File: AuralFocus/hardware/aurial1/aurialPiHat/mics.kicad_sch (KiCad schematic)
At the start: 7 parts, among them J1 Conn_01x05_Pin

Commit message: Muitas mudanças no circuito, clocks no stm32h7 e mais,
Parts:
- renumbered C2 to C1, C1 to C2, MK7 to MK1
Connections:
- net GND: no longer MK1.5 (GND)
- net VDD: no longer MK1.2 (VDD)
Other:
- note added: "Para SNR máximo do IM69D130 (69 dB(A)), adicione capacitor de bypass de 100 nF diretamente no pin VDD de cada microfone (<1 mm de distância) - o datasheet recomenda isso para melhor SNR."
- moved on the sheet: C1, C2, J1

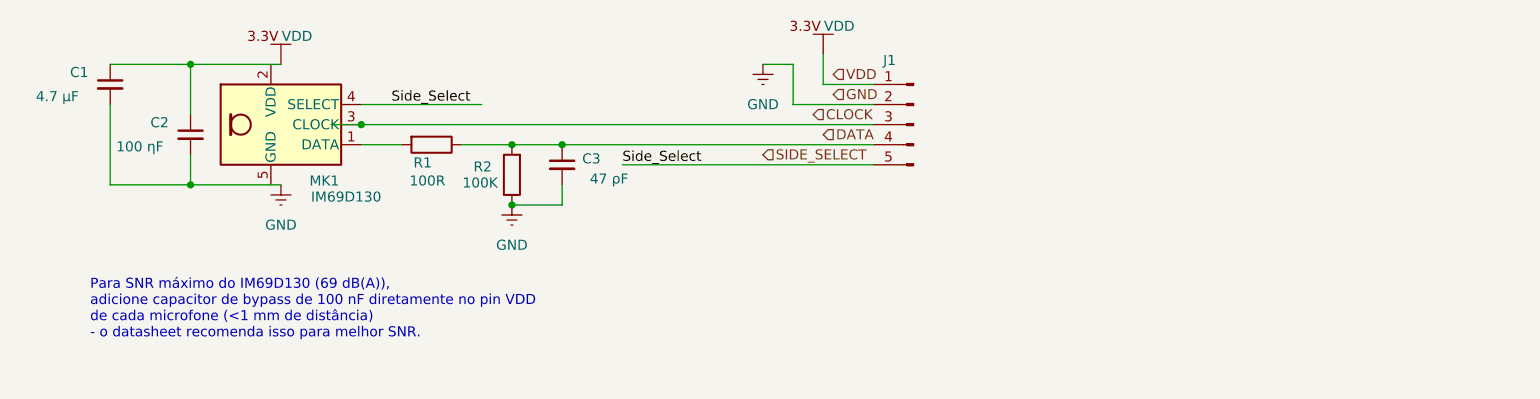
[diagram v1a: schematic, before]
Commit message: correções, VDD, VSS e outros pinos relevantes para contexto.
 ### Decoupling Strategy for STM32H753 Power Pins

 The STM32H753 microcontroller is a high-performance Cortex-M7 device operating at up to 480 MHz, with integrated USB High-Speed functionality. Such high-speed operation demands a robust power supply decoupling strategy to ensure signal integrity and minimize electromagnetic interference (EMI). Below is the detailed decoupling approach implemented in the AuralFocus HAT design:

 **1. Global Power Filtering**
 - **Ferrite Bead (FB3 - 600 Ω @ 100 MHz)**: placed on the main 3.3 V supply line feeding the STM32H753. This ferrite bead attenuates high-frequency noise originating from upstream sources (e.g., Raspberry Pi power supply, servo motors) before it reaches the microcontroller.
 - **Post-Ferrite Capacitor Bank**:
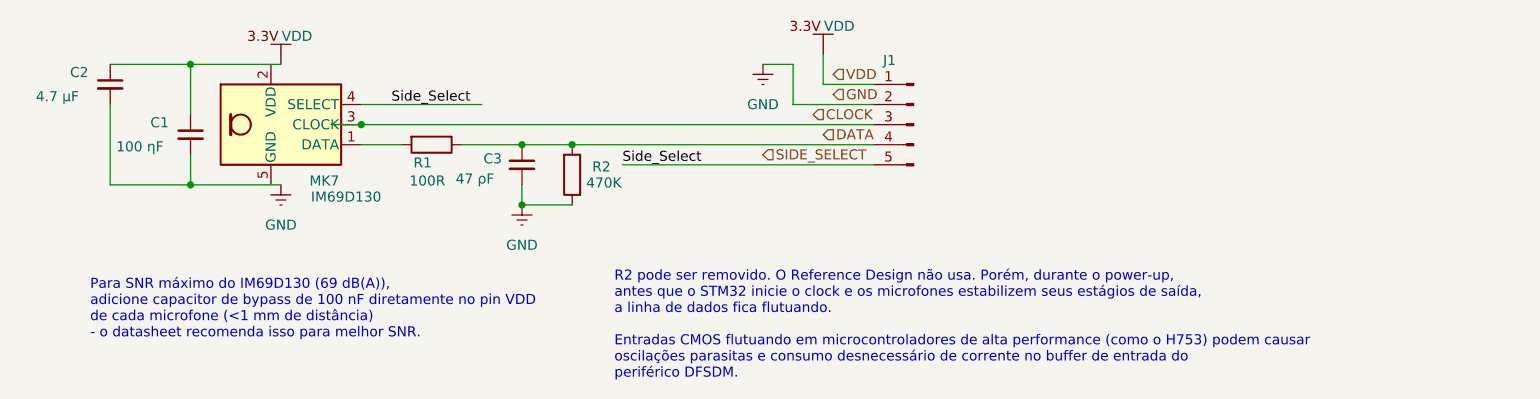
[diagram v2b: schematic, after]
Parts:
- R2: value 100K -> 470K
- renumbered C2 to C1, C1 to C2, MK1 to MK7
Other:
- note added: "R2 pode ser removido. O Reference Design não usa. Porém, durante o power-up, antes que o STM32 inicie o clock e os microfones estabilizem seus estágios de saída, a linha de dados fica flutuando. Entradas CMOS flutuando em microcontroladores de alta performance (como o H753) podem causar oscilações parasitas e consumo desnecessário de corrente no buffer de entrada do periférico DFSDM."
- moved on the sheet: C3, R2
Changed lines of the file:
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@@
 	(generator_version "9.0")
 	(paper "A4")
+	(text "R2 pode ser removido. O Reference Design não usa. Porém, durante o power-up, \nantes que o STM32 inicie o clock e os microfones estabilizem seus estágios de saída, \na linha de dados fica flutuando. \n\nEntradas CMOS flutuando em microcontroladores de alta performance (como o H753) podem causar \noscilações parasitas e consumo desnecessário de corrente no buffer de entrada do \nperiférico DFSDM."
+		(exclude_from_sim no)
+		(at 162.814 128.27 0)
+		(effects
+			(font
+				(size 1.27 1.27)
+			)
+			(justify left)
+		)
+	)
 	(text "Para SNR máximo do IM69D130 (69 dB(A)), \nadicione capacitor de bypass de 100 nF diretamente no pin VDD \nde cada microfone (<1 mm de distância) \n- o datasheet recomenda isso para melhor SNR."
 		(exclude_from_sim no)
@@
 	)
 	(junction
-		(at 149.86 113.03)
-		(diameter 0)
-		(color 0 0 0 0)
-	)
-	(junction
 		(at 109.22 95.25)
-		(diameter 0)
-		(color 0 0 0 0)
-	)
-	(junction
-		(at 156.21 105.41)
 		(diameter 0)
 		(color 0 0 0 0)
@@
 	)
 	(junction
-		(at 149.86 105.41)
+		(at 151.13 113.03)
 		(diameter 0)
 		(color 0 0 0 0)
@@
 		(color 0 0 0 0)
 	)
-	(wire
-		(pts
-			(xy 143.51 105.41) (xy 149.86 105.41)
+	(junction
+		(at 157.48 105.41)
+		(diameter 0)
+		(color 0 0 0 0)
+	)
+	(junction
+		(at 151.13 105.41)
+		(diameter 0)
+		(color 0 0 0 0)
+	)
+	(wire
+		(pts
+			(xy 143.51 105.41) (xy 151.13 105.41)
 		)
 		(stroke
@@
 	(wire
 		(pts
-			(xy 149.86 105.41) (xy 156.21 105.41)
+			(xy 151.13 105.41) (xy 157.48 105.41)
 		)
 		(stroke
@@
 	(wire
 		(pts
-			(xy 149.86 113.03) (xy 156.21 113.03)
-		)
-		(stroke
-			(width 0)
-			(type default)
-		)
-	)
-	(wire
-		(pts
 			(xy 99.06 110.49) (xy 109.22 110.49)
 		)
@@
 	(wire
 		(pts
-			(xy 156.21 110.49) (xy 156.21 113.03)
+			(xy 151.13 110.49) (xy 151.13 113.03)
+		)
+		(stroke
+			(width 0)
+			(type default)
+		)
+	)
+	(wire
+		(pts
+			(xy 157.48 105.41) (xy 195.58 105.41)
+		)
+		(stroke
+			(width 0)
+			(type default)
+		)
+	)
+	(wire
+		(pts
+			(xy 151.13 113.03) (xy 157.48 113.03)
 		)
 		(stroke
@@
 		(pts
 			(xy 130.81 100.33) (xy 146.05 100.33)
-		)
-		(stroke
-			(width 0)
-			(type default)
-		)
-	)
-	(wire
-		(pts
-			(xy 156.21 105.41) (xy 195.58 105.41)
 		)
 		(stroke
@@
 		(dnp no)
 		(fields_autoplaced yes)
-		(property "Reference" "#PWR?"
+		(property "Reference" "#PWR09"
 			(at 181.61 101.6 0)
 			(effects
@@
 		(dnp no)
 		(fields_autoplaced yes)
-		(property "Reference" "#PWR?"
+		(property "Reference" "#PWR08"
 			(at 189.23 97.79 0)
 			(effects
@@
 		(on_board yes)
 		(dnp no)
-		(property "Reference" "MK1"
+		(property "Reference" "MK7"
 			(at 128.016 109.982 0)
 			(effects
@@
 	(symbol
 		(lib_id "Device:R")
-		(at 149.86 109.22 180)
+		(at 157.48 109.22 0)
+		(mirror x)
 		(unit 1)
 		(exclude_from_sim no)
@@
 		(dnp no)
 		(property "Reference" "R2"
-			(at 147.32 108.204 0)
+			(at 160.02 108.204 0)
 			(effects
 				(font
@@
 			)
 		)
-		(property "Value" "100K"
-			(at 148.082 110.236 0)
+		(property "Value" "470K"
+			(at 159.258 110.236 0)
 			(effects
 				(font
@@
 		)
 		(property "Footprint" ""
-			(at 151.638 109.22 90)
+			(at 155.702 109.22 90)
 			(effects
 				(font
@@
 		)
 		(property "Datasheet" "~"
-			(at 149.86 109.22 0)
+			(at 157.48 109.22 0)
 			(effects
 				(font
@@
 		)
 		(property "Description" "Resistor"
-			(at 149.86 109.22 0)
+			(at 157.48 109.22 0)
 			(effects
 				(font
@@
 		(on_board yes)
 		(dnp no)
-		(property "Reference" "J?"
+		(property "Reference" "J1"
 			(at 197.612 94.742 0)
 			(effects
@@
 	(symbol
 		(lib_id "power:GNDREF")
-		(at 149.86 113.03 0)
+		(at 151.13 113.03 0)
 		(unit 1)
 		(exclude_from_sim no)
@@
 		(dnp no)
 		(fields_autoplaced yes)
-		(property "Reference" "#PWR?"
-			(at 149.86 119.38 0)
+		(property "Reference" "#PWR06"
+			(at 151.13 119.38 0)
 			(effects
 				(font
@@
 		)
 		(property "Value" "GND"
-			(at 149.86 118.11 0)
+			(at 151.13 118.11 0)
 			(effects
 				(font
@@
 		)
 		(property "Footprint" ""
-			(at 149.86 113.03 0)
+			(at 151.13 113.03 0)
 			(effects
 				(font
@@
 		)
 		(property "Datasheet" ""
-			(at 149.86 113.03 0)
+			(at 151.13 113.03 0)
 			(effects
 				(font
@@
 		)
 		(property "Description" "Power symbol creates a global label with name \"GNDREF\" , reference supply ground"
-			(at 149.86 113.03 0)
+			(at 151.13 113.03 0)
 			(effects
 				(font
@@
 		(on_board yes)
 		(dnp no)
-		(property "Reference" "C2"
+		(property "Reference" "C1"
 			(at 104.14 102.616 0)
 			(effects
@@
 		(dnp no)
 		(fields_autoplaced yes)
-		(property "Reference" "#PWR?"
+		(property "Reference" "#PWR07"
 			(at 120.65 99.06 0)
 			(effects
@@
 		(dnp no)
 		(fields_autoplaced yes)
-		(property "Reference" "#PWR?"
+		(property "Reference" "#PWR05"
 			(at 120.65 116.84 0)
 			(effects
@@
 	(symbol
 		(lib_id "Device:C_Small")
-		(at 156.21 107.95 0)
+		(at 151.13 107.95 0)
+		(mirror y)
 		(unit 1)
 		(exclude_from_sim no)
@@
 		(dnp no)
 		(property "Reference" "C3"
-			(at 158.75 107.188 0)
+			(at 148.59 107.188 0)
 			(effects
 				(font
@@
 		)
 		(property "Value" "47 ρF"
-			(at 164.592 109.728 0)
+			(at 142.748 109.728 0)
 			(effects
 				(font
@@
 		)
 		(property "Footprint" ""
-			(at 156.21 107.95 0)
+			(at 151.13 107.95 0)
 			(effects
 				(font
@@
 		)
 		(property "Datasheet" "~"
-			(at 156.21 107.95 0)
+			(at 151.13 107.95 0)
 			(effects
 				(font
@@
 		)
 		(property "Description" "Unpolarized capacitor, small symbol"
-			(at 156.21 107.95 0)
+			(at 151.13 107.95 0)
 			(effects
 				(font
@@
 		(on_board yes)
 		(dnp no)
-		(property "Reference" "C1"
+		(property "Reference" "C2"
 			(at 93.98 96.266 0)
 			(effects
